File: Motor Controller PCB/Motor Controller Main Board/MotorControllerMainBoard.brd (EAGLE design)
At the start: 100 x 100 mm, 99 parts, among them T1 TEENSY_3.1_ALL_PINS

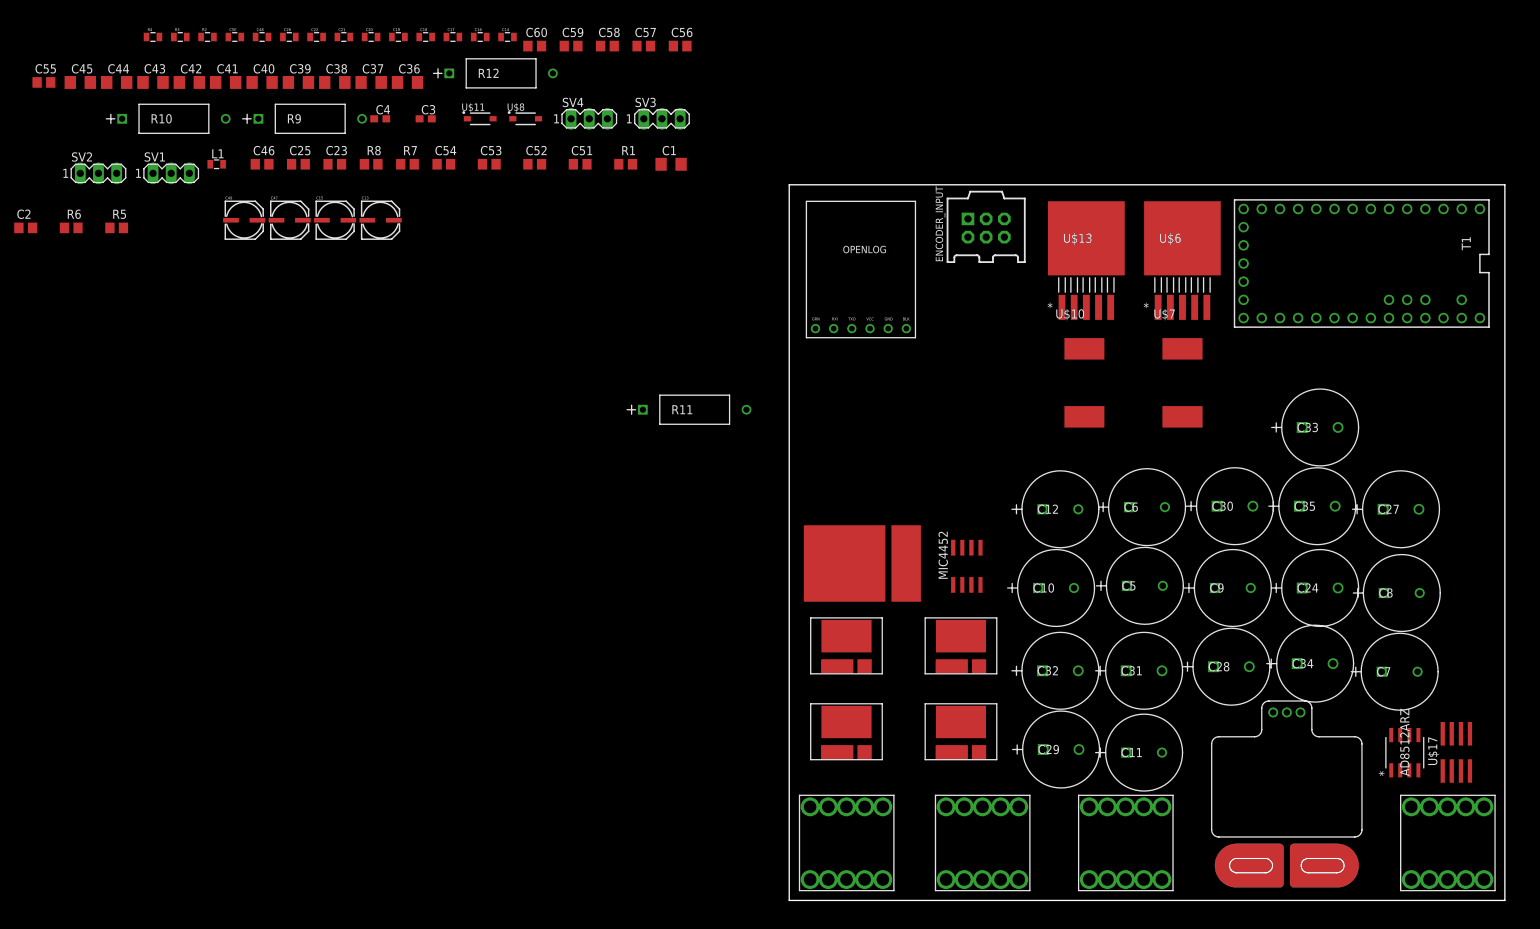
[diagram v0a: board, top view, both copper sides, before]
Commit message: Board work and removed some caps
-Removed 2 caps from 5V reg and 12V and -12V reg
-Removed 5 caps from input filter and 5 ceramics
-Larger components are in place, I started wiring the input caps.
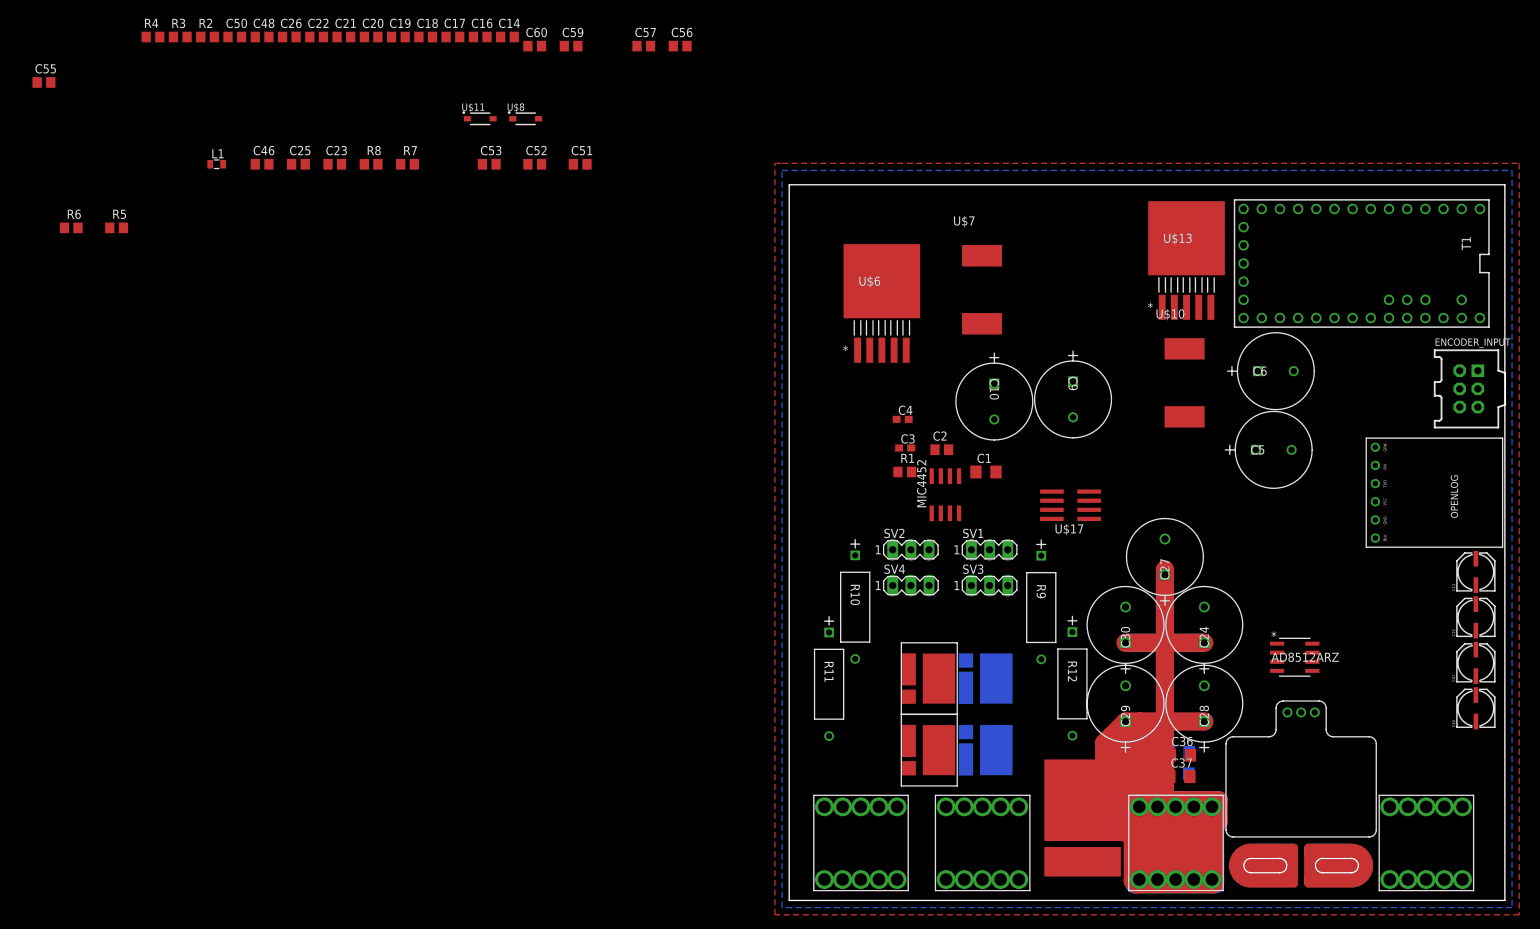
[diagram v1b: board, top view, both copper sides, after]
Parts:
- removed C11, C12, C7, C8: EEUFR1H221B, MotorControllerEagleLibrary:CAP_PAN_10X16
- removed C31, C32, C33, C34, C35: EEU-FR1H331L, MotorControllerEagleLibrary:CAP_EEUFC_10X25
- removed C41, C42, C43, C44, C45: (no value), resistor:C1206
- removed C54: 10uF, resistor:C0805
- removed C58: (no value), resistor:C0805
- C14, C16, C17, C18, C19, C20, C21, C22, C26, C48, C50: device SparkFun-Capacitors:0805 -> resistor:C0805
- R2, R3, R4: device SparkFun-Passives:0805 -> resistor:C0805
- moved C49 185.1 mm to (95.8, 26.8), turned to 90 degrees
- moved C47 176.9 mm to (95.8, 33.1), turned to 90 degrees
- moved C15 168.7 mm to (95.8, 39.5), turned to 90 degrees
- moved C13 160.7 mm to (95.8, 45.9), turned to 90 degrees
- moved C39 156.4 mm to (54.4, 17.7), flipped to the bottom, turned to 180 degrees
- moved C40 155.8 mm to (49.4, 18.8), flipped to the bottom
- moved C38 150.6 mm to (54.5, 20.7), flipped to the bottom, turned to 180 degrees
- moved C37 148.9 mm to (54.6, 17.3)
- moved C36 143.2 mm to (54.7, 20.3)
- moved C2 131.7 mm to (21.3, 63.0)
- moved SV1 125.9 mm to (28.0, 49.0)
- moved SV2 125.1 mm to (17.0, 49.0)
- moved R9 121.3 mm to (35.2, 33.7), turned to 270 degrees
- moved R12 117.6 mm to (39.6, 23.0), turned to 270 degrees
- moved R10 115.9 mm to (9.22, 33.7), turned to 270 degrees
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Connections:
- net 12V_POWER_REGULATED: no longer C7.1, C8.1
- net 5V_POWER_REGULATED: no longer C11.1, C12.1
- net GND: no longer C11.2, C12.2, C31.2, C32.2, C33.2, C34.2, C35.2, C41.2, C42.2, C43.2, C44.2, C45.2, C58.2, C7.2, C8.2
- net MAIN_POWER_IN(+): no longer C31.1, C32.1, C33.1, C34.1, C35.1, C41.1, C42.1, C43.1, C44.1, C45.1
- net N$14: no longer C54.1
- net N$15: no longer C54.2
- net OUTPUT_12NEG: no longer C58.1
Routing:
- net MAIN_POWER_IN(+): track 0.00 -> 472.9 mm
- added copper zone on layer 1, net GND
- added copper zone on layer 16, net GND

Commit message: Placed all components on board
-They just need wiring.
-Yes I know it looks sloppy, but we need a quick prototype.
-Final version of the board will have more thought into component
placement
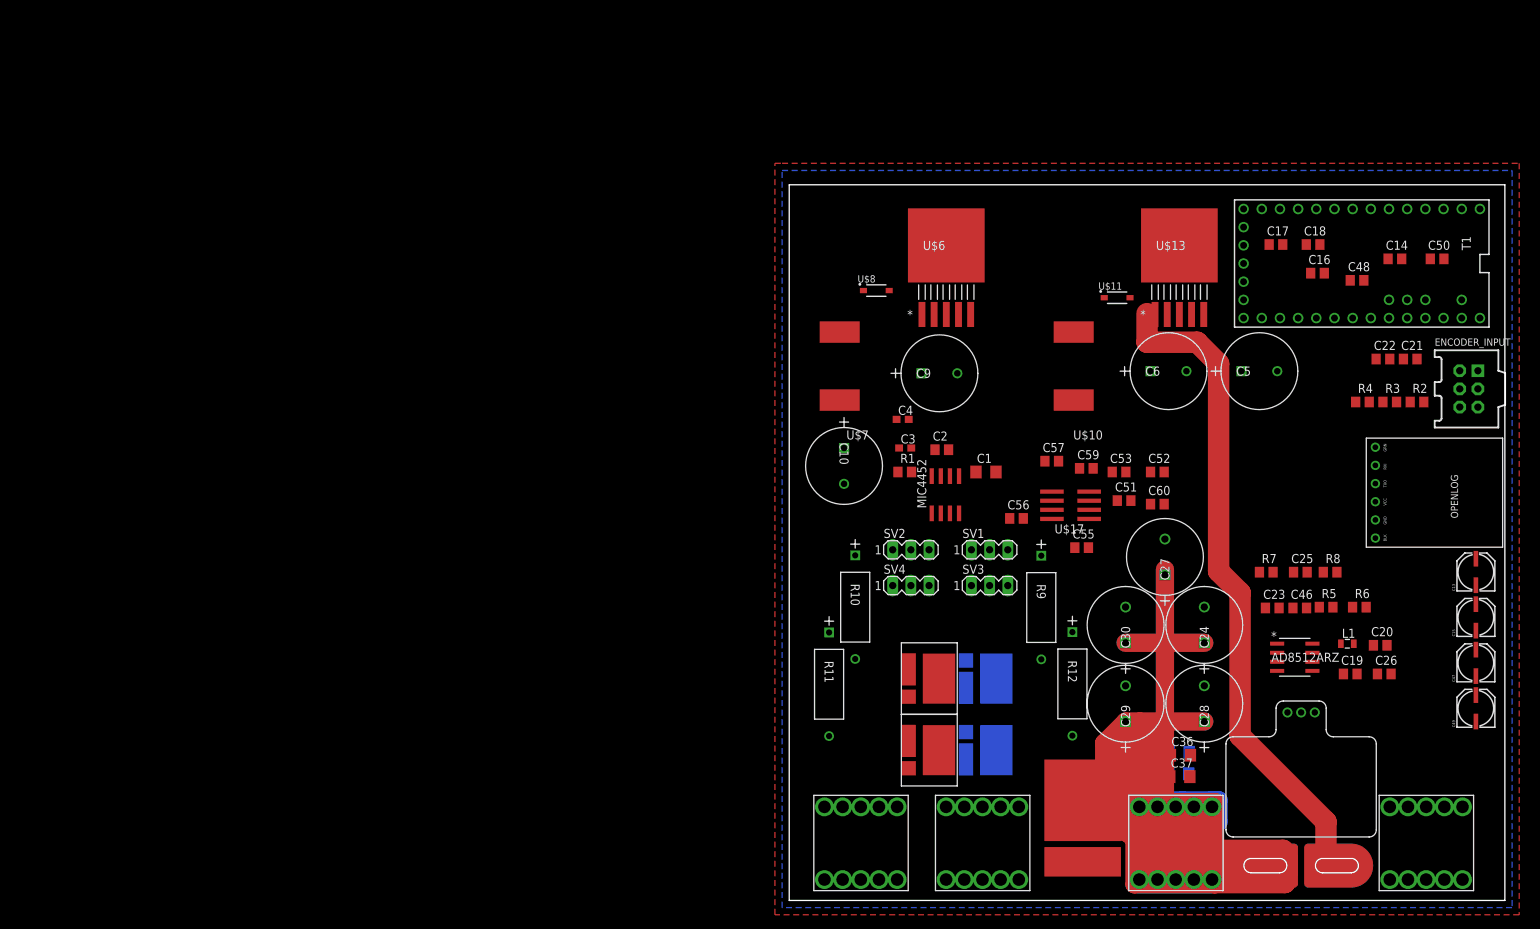
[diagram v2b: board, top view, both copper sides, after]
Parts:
- R2, R3, R4: device resistor:C0805 -> resistor:R0805
- moved R6 187.6 mm to (79.7, 41.0)
- moved R5 177.1 mm to (75.0, 41.0)
- moved C26 177.0 mm to (83.2, 31.6)
- moved R2 176.5 mm to (87.7, 69.7)
- moved R3 176.5 mm to (83.9, 69.7)
- moved R4 176.5 mm to (80.1, 69.7)
- moved L1 171.6 mm to (78.0, 35.9)
- moved C50 170.8 mm to (90.5, 89.7)
- moved C20 164.6 mm to (82.6, 35.6)
- moved C19 160.0 mm to (78.4, 31.6)
- moved C55 158.9 mm to (40.9, 49.3)
- moved C46 157.7 mm to (71.3, 40.9)
- moved C48 156.7 mm to (79.3, 86.7)
- moved C21 155.6 mm to (86.8, 75.7)
- moved C22 155.6 mm to (83.0, 75.7)
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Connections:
- net MAIN_POWER_IN(+) renamed INPUT_POWER(+)
- net SAFE_POWER renamed POWER_INPUT(+)
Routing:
- net INPUT_POWER(+): track 472.9 -> 312.4 mm
- net MAIN_POWER_IN(+): track 0.00 -> 140.2 mm
- net POWER_INPUT(+): track 0.00 -> 91.5 mm
- net N$16: track 0.00 -> 4.24 mm

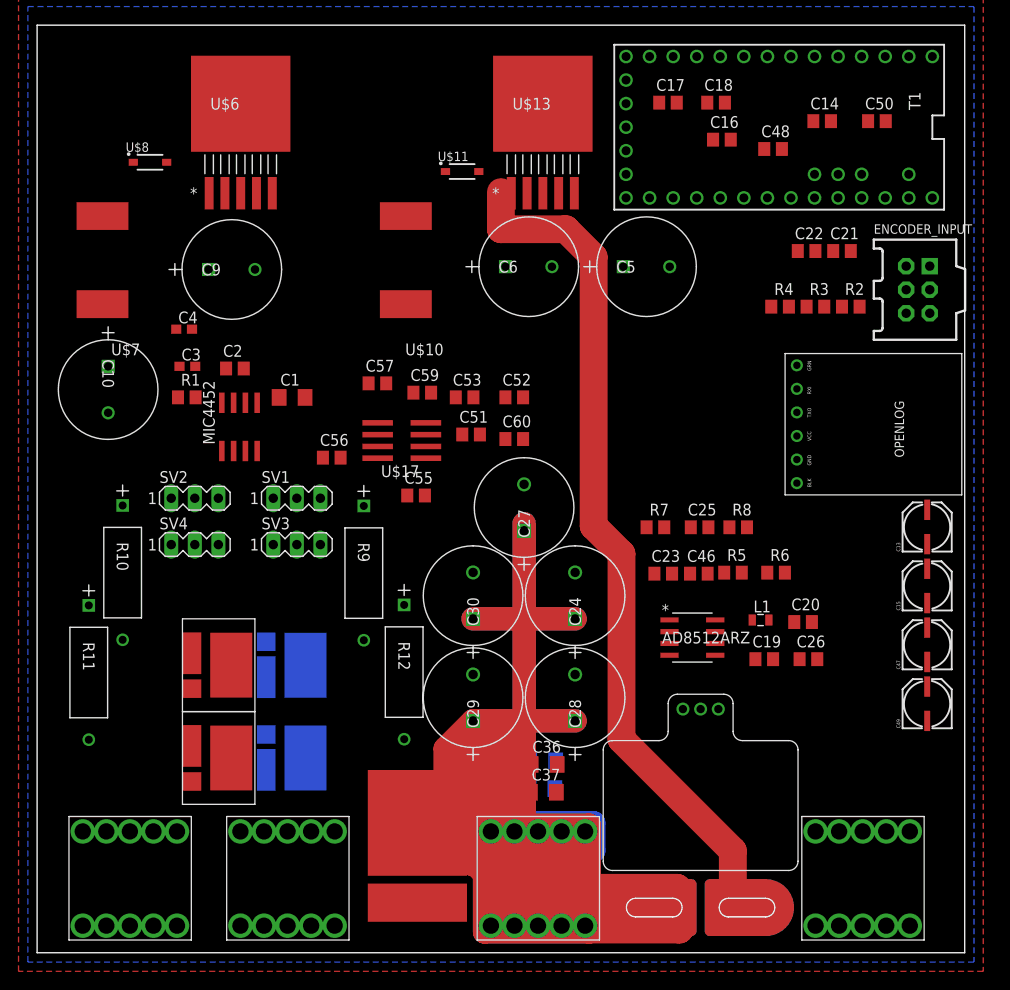
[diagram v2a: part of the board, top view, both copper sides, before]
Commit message: Routed majority of the power components
-Only thing left is stuff connected to teensy and other things i missed
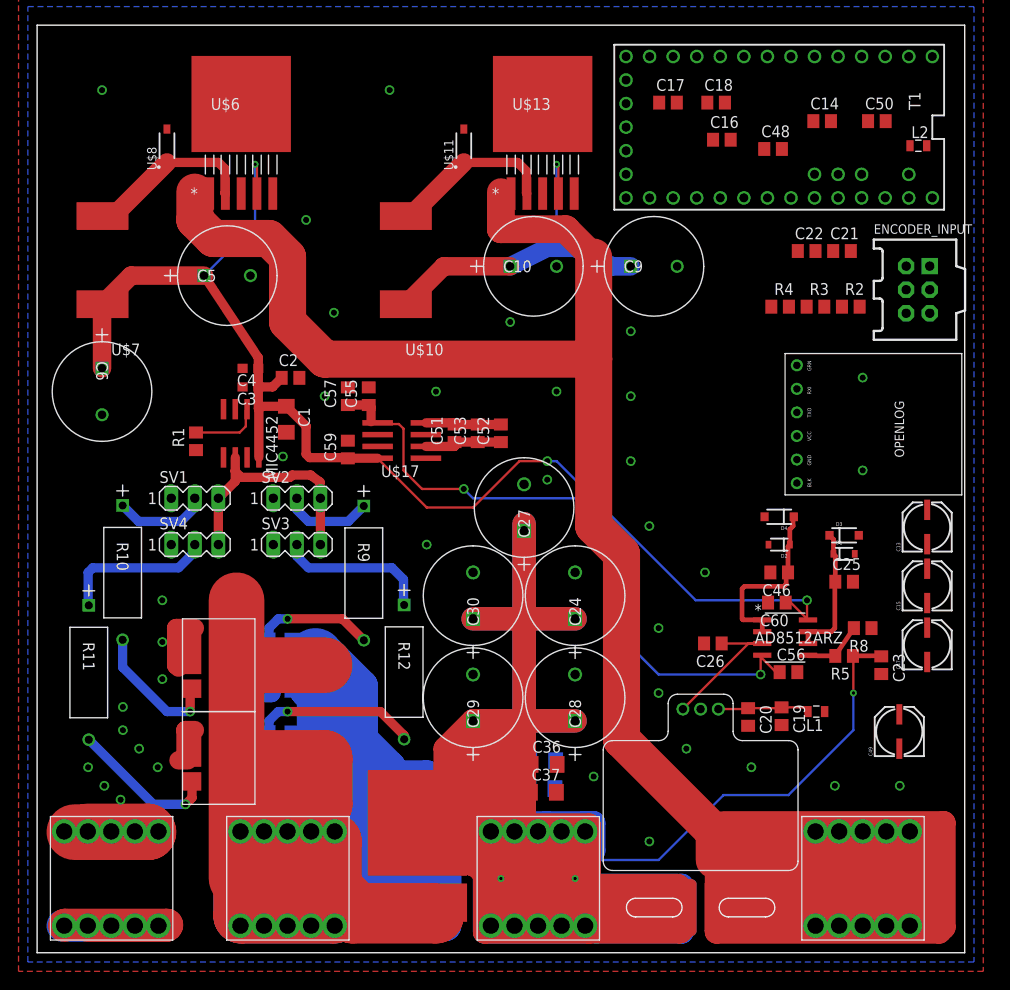
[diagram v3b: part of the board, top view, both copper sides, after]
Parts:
- removed R6: 100k, rcl:R0805
- removed R7: 10k, rcl:R0805
- added D1, D2: BAT20J, SparkFun-DiscreteSemi:SOD-323
- added D3, D4: 16V, SparkFun-DiscreteSemi:SOD-123
- added L2: 42nH, SparkFun (2015_10_14 22_27_04 UTC):0805
- C55, C56, C57, C59, C60: value (none) -> 10uF
- R5: value 100k -> 90.9k
- moved C56 54.4 mm to (81.0, 30.2)
- moved C6 51.1 mm to (7.00, 58.0), turned to 270 degrees
- moved C10 50.9 mm to (56.0, 74.0), turned to 0 degrees
- moved C9 45.5 mm to (69.0, 74.0)
- moved C5 45.2 mm to (23.0, 73.0)
- moved C60 33.4 mm to (79.8, 37.8), turned to 180 degrees
- moved C23 25.5 mm to (91.0, 31.0), turned to 270 degrees
- moved R8 17.3 mm to (89.0, 35.0), turned to 180 degrees
- moved C25 16.6 mm to (87.0, 40.0)
- moved R5 15.0 mm to (87.0, 32.0), turned to 180 degrees
- moved C55 11.9 mm to (35.8, 60.0), turned to 90 degrees
- moved C20 11.8 mm to (76.7, 25.4), turned to 270 degrees
- moved L1 11.6 mm to (84.0, 26.0), turned to 180 degrees
- moved SV1 11.0 mm to (17.0, 49.0)
- moved SV2 11.0 mm to (28.0, 49.0)
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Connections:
- new net N$13: R9.1, SV2.2
- net 3.3V_POWER_REGULATED: now also L2.2; no longer C17.1, C18.1, T1.AREF
- net CURRENT_FEEDBACK: now also D2.C, D4.C
- net FET_DRIVER_SIGNAL: no longer R9.1, SV2.2
- net GND: now also D1.A, D2.A, D3.A, D4.A; no longer R6.1
- net INPUT_POWER(+): now also C23.1, R5.1
- net MOTOR_OUTPUT_(+): now also U$13.1, U$6.1
- net N$9: now also C17.1, C18.1, L2.1, T1.AREF; no longer AD8512ARZ.6, R6.2, R7.1
- net POWER_INPUT(+): no longer C23.1, R5.1, U$13.1, U$6.1
- net SUPPLY_VOLTAGE: now also AD8512ARZ.6, D1.C, D3.C; no longer R7.2
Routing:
- net MOTOR_OUTPUT_(+): track 0.00 -> 363.5 mm
- net MOTOR_OUTPUT_(--): track 0.00 -> 358.6 mm
- net INPUT_POWER(+): track 312.4 -> 573.8 mm, vias 0 -> 3
- net 12V_POWER_REGULATED: track 0.00 -> 141.1 mm, vias 0 -> 3
- net MAIN_POWER_IN(+): track 140.2 -> 0.00 mm
- net POWER_INPUT(+): track 91.5 -> 0.00 mm
- net GND: track 0.00 -> 81.3 mm, vias 0 -> 36
- net OUTPUT_12NEG: track 0.00 -> 70.8 mm, vias 0 -> 2
- net 5V_POWER_REGULATED: track 0.00 -> 39.1 mm, vias 0 -> 1
- net FET_DRIVER_SIGNAL: track 0.00 -> 26.9 mm
- net CURRENT_FEEDBACK: track 0.00 -> 19.3 mm
- net N$12: track 0.00 -> 18.7 mm, vias 0 -> 1
- net N$1: track 0.00 -> 18.6 mm
- net N$4: track 0.00 -> 18.2 mm
- net N$8: track 0.00 -> 16.8 mm
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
